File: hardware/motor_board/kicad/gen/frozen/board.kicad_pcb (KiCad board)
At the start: 6 copper layers, 75 x 35 mm, 237 parts, among them J1 BOOMELE_1.27-2x10P, J2 WAFER-SH1.0-6PWB, J3 WAFER-SH1.0-6PWB, J4 S5B-XH-A, Q1 HYG015N04LS1C2, Q2 HYG015N04LS1C2, Q3 HYG015N04LS1C2, Q4 HYG015N04LS1C2, Q5 HYG015N04LS1C2, Q6 HYG015N04LS1C2, Q7 HYG015N04LS1C2, Q8 HYG015N04LS1C2, U1 STM32G474RET6, U10 SN74LVC3G17DCUR, U11 TPS22945DCKR, U12 TPS22945DCKR, U13 LM74502DDFR, U14 74LVC1G17SE-7, U2 DRV8323RHRGZR, U3 DRV8316CRRGFR, U4 DRV8316CRRGFR, U5 AP2112K-3.3TRG1, U6 SN74LVC08APWR, U7 INA239AIDGSR, U8 BQ76907RGRR, U9 SN74LVC3G17DCUR

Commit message: tail: +3V3 pour on L4 spare area + drop vias for stranded +3V3 pads; zone op; tail_auto (DRC opens -> router requests); DRC 0, 84 open
Co-Authored-By: Claude Opus 5.5 (1M context) <noreply@anthropic.com>
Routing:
- net +3V3: track 146.5 -> 159.8 mm, vias 13 -> 23
- added copper zone on In3.Cu, net +3V3

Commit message: tail: GND pour-island stitch vias/drops (islands.py finds unanchored fills); DRC 0, 79 open
Co-Authored-By: Claude Opus 5.5 (1M context) <noreply@anthropic.com>
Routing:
- net GND: track 151.2 -> 155.1 mm, vias 198 -> 203
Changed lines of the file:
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@@
+	)
+	(segment
+		(start 161.75 96.6)
+		(end 161.8 96.65)
+		(width 0.25)
+		(layer "F.Cu")
+		(net "GND")
 	)
 	(segment
@@
 	)
 	(segment
+		(start 161.21 96.6)
+		(end 161.75 96.6)
+		(width 0.25)
+		(layer "F.Cu")
+		(net "GND")
+	)
+	(segment
 		(start 161.5 98.68)
 		(end 161.5 99.2)
@@
 	)
 	(segment
+		(start 147.85 103.85)
+		(end 148.6 103.85)
+		(width 0.25)
+		(layer "F.Cu")
+		(net "GND")
+	)
+	(segment
 		(start 139 103.85)
 		(end 138.9 103.75)
@@
 	)
 	(via
+		(at 139.384 104.195)
+		(size 0.4)
+		(drill 0.2)
+		(layers "F.Cu" "B.Cu")
+		(net "GND")
+	)
+	(via
 		(at 168.9 102.15)
 		(size 0.45)
@@
 	)
 	(via
+		(at 148.6 103.85)
+		(size 0.4)
+		(drill 0.2)
+		(layers "F.Cu" "B.Cu")
+		(net "GND")
+	)
+	(via
 		(at 154.174999 93.675)
 		(size 0.6)
@@
 	)
 	(via
+		(at 148.015 91.094)
+		(size 0.4)
+		(drill 0.2)
+		(layers "F.Cu" "B.Cu")
+		(net "GND")
+	)
+	(via
 		(at 167.15 88.15)
 		(size 0.45)
@@
 	)
 	(via
+		(at 138.05 88)
+		(size 0.4)
+		(drill 0.2)
+		(layers "F.Cu" "B.Cu")
+		(net "GND")
+	)
+	(via
 		(at 131.219999 92.695)
 		(size 0.45)
@@
 		(size 0.45)
 		(drill 0.25)
+		(layers "F.Cu" "B.Cu")
+		(net "GND")
+	)
+	(via
+		(at 161.8 96.65)
+		(size 0.4)
+		(drill 0.2)
 		(layers "F.Cu" "B.Cu")
 		(net "GND")
@@
 	)
 	(segment
+		(start 138.1 88.05)
+		(end 138.05 88)
+		(width 0.25)
+		(layer "B.Cu")
+		(net "GND")
+	)
+	(segment
 		(start 132.25 86.6)
 		(end 131.5 87.35)
@@
 	)
 	(segment
+		(start 138.75 89.2)
+		(end 138.1 88.55)
+		(width 0.25)
+		(layer "B.Cu")
+		(net "GND")
+	)
+	(segment
 		(start 149.55 97.6)
 		(end 149.5 97.6)
@@
 	)
 	(segment
+		(start 138.1 88.55)
+		(end 138.1 88.05)
+		(width 0.25)
+		(layer "B.Cu")
+		(net "GND")
+	)
+	(segment
 		(start 103.5 88.8125)
 		(end 102.23 88.1125)
@@
 		(layer "B.Cu")
 		(net "GND")
+	)
+	(segment
+		(start 138.75 90.325)
+		(end 138.75 89.2)
+		(width 0.25)
+		(layer "B.Cu")
+		(net "GND")

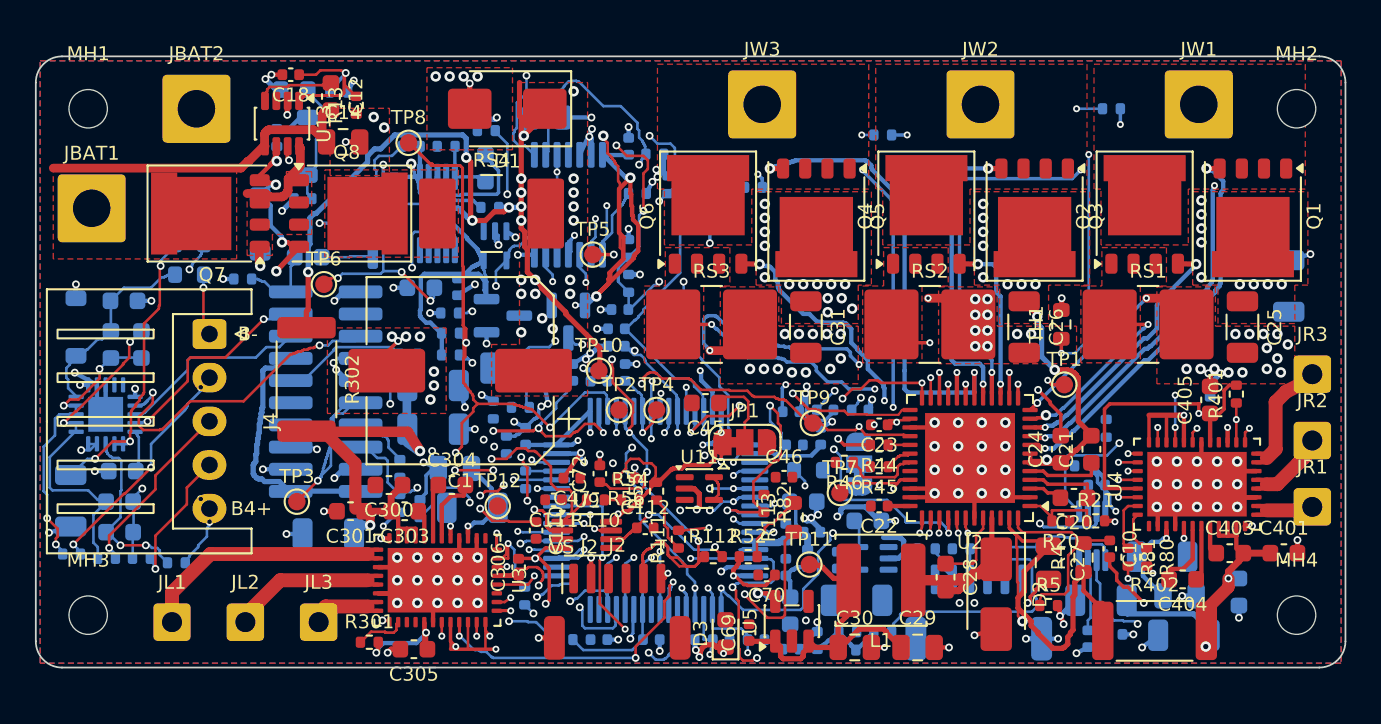
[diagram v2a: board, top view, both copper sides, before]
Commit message: tail: rail ties (router ignore_pours flag for short ties through power pours); DRC 0, 75 open
Co-Authored-By: Claude Opus 5.5 (1M context) <noreply@anthropic.com>
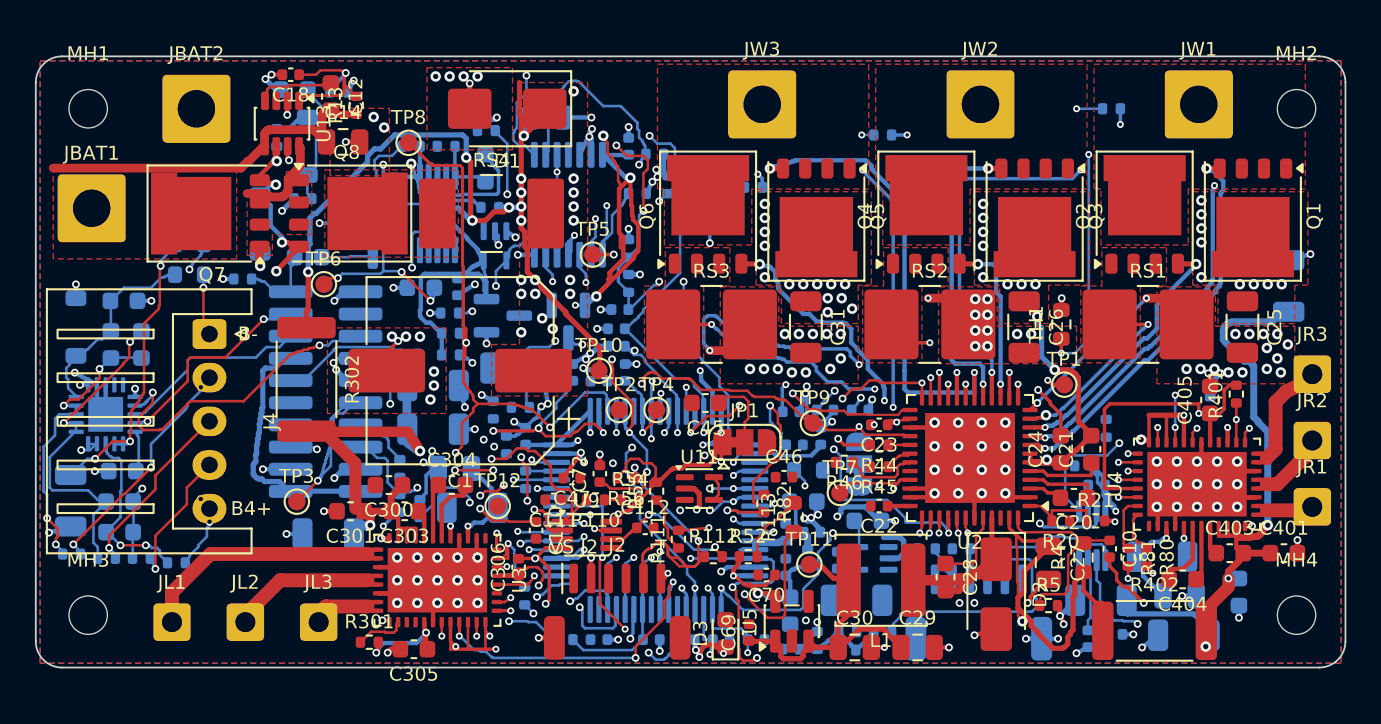
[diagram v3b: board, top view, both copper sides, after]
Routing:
- net /drive_right/R_VM: track 13.9 -> 33.4 mm, vias 2 -> 3
- net +3V3: track 159.8 -> 168.1 mm, vias 23 -> 24
- net /power/BAT_IN: track 19.6 -> 21.2 mm
